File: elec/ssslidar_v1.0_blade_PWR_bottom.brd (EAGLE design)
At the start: 12 x 7 mm, 25 parts, among them P10 PIN_SMD_1X1_RECT, P11 PIN_SMD_1X2, P12 PIN_SMD_1X1_RECT, P13 PIN_SMD_1X1_RECT, P15 PIN_SMD_0.8X1_RECT, P16 PIN_SMD_1X1_RECT, P17 PIN_SMD_1X2, P18 PIN_SMD_0.8X1_RECT, P19 PIN_SMD_0.8X1_RECT, P2 PIN_SMD_1X1_RECT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

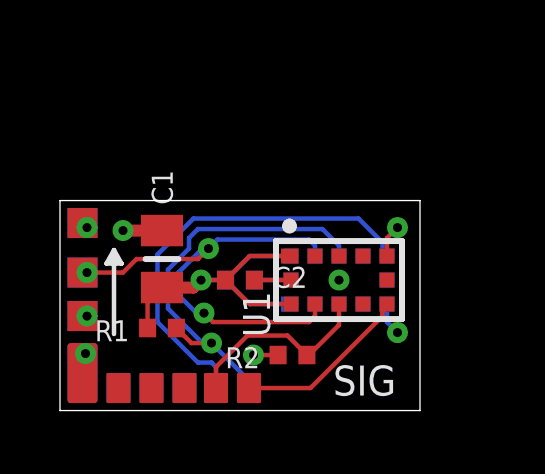
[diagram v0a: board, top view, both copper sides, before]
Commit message: Separated blades into bottom and top, since the bottom ones need to be taller to avoid seeing the Main PCB, or the screws...
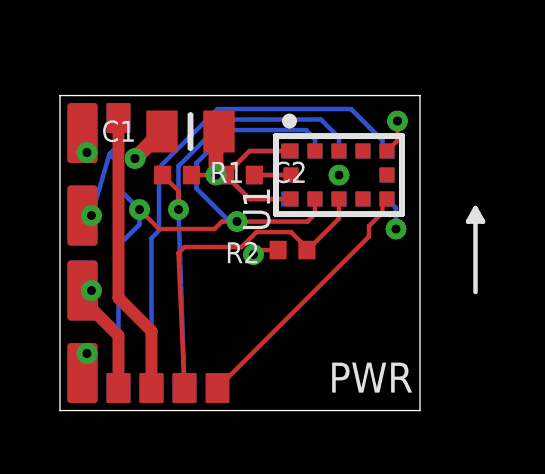
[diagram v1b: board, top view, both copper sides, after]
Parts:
- removed P19, P20, P23: PIN_SMD_0.8X1_RECT, Xevelabs:PIN_SMD_0.8X1_RECT
- added P1, P3: PIN_SMD_0.8X1_RECT, Xevelabs:PIN_SMD_0.8X1_RECT
- P10, P12, P13, P16, P2, P9: value PIN_SMD_1X1_RECT -> PIN_SMD_1X2; device Xevelabs:PIN_SMD_1X1_RECT -> Xevelabs:PIN_SMD_1X2
- moved P18 9.26 mm to (1.95, 9.75), turned to 90 degrees
- moved R1 5.12 mm to (3.90, 7.85), turned to 0 degrees
- moved C1 4.35 mm to (4.35, 9.30), turned to 180 degrees
- moved C2 3.50 mm to (6.00, 7.85)
- moved C3 3.50 mm to (6.00, 7.85)
- moved U1 3.50 mm to (9.30, 7.85)
- moved U2 3.50 mm to (9.30, 7.85)
- moved R2 3.50 mm to (7.75, 5.35)
- moved P2 3.00 mm to (0.75, 9.25), turned to 0 degrees
- moved P9 3.00 mm to (0.75, 9.25)
- moved P7 2.15 mm to (3.05, 0.75)
- moved P5 2.15 mm to (4.15, 0.75)
- moved P10 1.90 mm to (0.75, 6.50)
- moved P12 1.90 mm to (0.75, 6.50)
- moved P8 1.10 mm to (1.95, 0.75), flipped to the top, turned to 90 degrees
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- renumbered P15 to P14
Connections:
- new net VDD_PASS: P1.PIN, P14.PIN
- net GND: now also P2.P$1, P9.P$1; no longer P2.PIN, P9.PIN
- net SCL: now also P10.P$1, P12.P$1, P18.PIN, P3.PIN; no longer P10.PIN, P12.PIN
- net VDD: now also P13.P$1, P16.P$1, P8.PIN; no longer P13.PIN, P16.PIN
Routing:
- net SCL: track 16.3 -> 27.0 mm
- net VDD_PASS: track 0.00 -> 9.46 mm
- net SDA1: track 6.62 -> 11.5 mm
- net INT1: track 5.91 -> 8.64 mm
- net VDD: track 17.9 -> 20.6 mm
- net INT2: track 14.4 -> 16.6 mm
- net SDA2: track 13.7 -> 15.5 mm
- net GND: track 5.66 -> 7.16 mm
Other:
- board size 12 x 7 mm -> 12 x 10.5 mm
- board text added: "PWR"
- board text removed: "SIG"

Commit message: Blades redesign done.
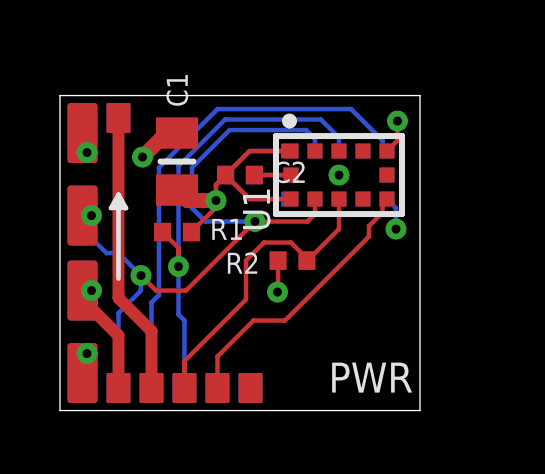
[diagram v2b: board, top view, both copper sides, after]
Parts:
- added P15, P19, P20: PIN_SMD_0.8X1_RECT, Xevelabs:PIN_SMD_0.8X1_RECT
- moved R1 1.90 mm to (3.90, 5.95)
- moved C1 1.10 mm to (3.90, 8.30), turned to 90 degrees
- moved R2 0.35 mm to (7.75, 5.00)
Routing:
- net VDD: track 20.6 -> 22.3 mm
- net SCL: track 27.0 -> 28.4 mm
- net SDA1: track 11.5 -> 10.2 mm
- net INT1: track 8.64 -> 9.26 mm

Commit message: Updated all libs.
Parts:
- turned P10 to 90 degrees
- turned P11 to 270 degrees
- turned P12 to 90 degrees
- turned P13 to 270 degrees
- turned P16 to 270 degrees
- turned P17 to 270 degrees
- turned P2 to 270 degrees
- turned P9 to 90 degrees
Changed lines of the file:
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@@
 <element name="U2" library="VL53L0X" package="VL53L0X" value="VL53L0X" x="9.3" y="7.85" rot="MR270"/>
 <element name="P1" library="Xevelabs" package="PIN_SMD_0.8X1_RECT" value="PIN_SMD_0.8X1_RECT" x="1.95" y="9.75" rot="R90"/>
-<element name="P2" library="Xevelabs" package="PIN_SMD_1X2" value="PIN_SMD_1X2" x="0.75" y="9.25" rot="MR0"/>
+<element name="P2" library="Xevelabs" package="PIN_SMD_1X2" value="PIN_SMD_1X2" x="0.75" y="9.25" rot="MR270"/>
 <element name="P3" library="Xevelabs" package="PIN_SMD_0.8X1_RECT" value="PIN_SMD_0.8X1_RECT" x="1.95" y="0.75" rot="MR90"/>
 <element name="P4" library="Xevelabs" package="PIN_SMD_0.8X1_RECT" value="PIN_SMD_0.8X1_RECT" x="4.15" y="0.75" rot="R90"/>
@@
 <element name="P6" library="Xevelabs" package="PIN_SMD_0.8X1_RECT" value="PIN_SMD_0.8X1_RECT" x="5.25" y="0.75" rot="R90"/>
 <element name="P7" library="Xevelabs" package="PIN_SMD_0.8X1_RECT" value="PIN_SMD_0.8X1_RECT" x="3.05" y="0.75" rot="MR90"/>
-<element name="P16" library="Xevelabs" package="PIN_SMD_1X2" value="PIN_SMD_1X2" x="0.75" y="4" rot="R180"/>
-<element name="P17" library="Xevelabs" package="PIN_SMD_1X2" value="PIN_SMD_1X2" x="0.75" y="1.25" rot="MR0"/>
+<element name="P16" library="Xevelabs" package="PIN_SMD_1X2" value="PIN_SMD_1X2" x="0.75" y="4" rot="R270"/>
+<element name="P17" library="Xevelabs" package="PIN_SMD_1X2" value="PIN_SMD_1X2" x="0.75" y="1.25" rot="MR270"/>
 <element name="P18" library="Xevelabs" package="PIN_SMD_0.8X1_RECT" value="PIN_SMD_0.8X1_RECT" x="1.95" y="9.75" rot="MR90"/>
 <element name="P8" library="Xevelabs" package="PIN_SMD_0.8X1_RECT" value="PIN_SMD_0.8X1_RECT" x="1.95" y="0.75" rot="R90"/>
-<element name="P9" library="Xevelabs" package="PIN_SMD_1X2" value="PIN_SMD_1X2" x="0.75" y="9.25"/>
-<element name="P10" library="Xevelabs" package="PIN_SMD_1X2" value="PIN_SMD_1X2" x="0.75" y="6.5" rot="MR180"/>
-<element name="P11" library="Xevelabs" package="PIN_SMD_1X2" value="PIN_SMD_1X2" x="0.75" y="1.25" rot="R180"/>
-<element name="P12" library="Xevelabs" package="PIN_SMD_1X2" value="PIN_SMD_1X2" x="0.75" y="6.5"/>
-<element name="P13" library="Xevelabs" package="PIN_SMD_1X2" value="PIN_SMD_1X2" x="0.75" y="4" rot="MR0"/>
+<element name="P9" library="Xevelabs" package="PIN_SMD_1X2" value="PIN_SMD_1X2" x="0.75" y="9.25" rot="R90"/>
+<element name="P10" library="Xevelabs" package="PIN_SMD_1X2" value="PIN_SMD_1X2" x="0.75" y="6.5" rot="MR90"/>
+<element name="P11" library="Xevelabs" package="PIN_SMD_1X2" value="PIN_SMD_1X2" x="0.75" y="1.25" rot="R270"/>
+<element name="P12" library="Xevelabs" package="PIN_SMD_1X2" value="PIN_SMD_1X2" x="0.75" y="6.5" rot="R90"/>
+<element name="P13" library="Xevelabs" package="PIN_SMD_1X2" value="PIN_SMD_1X2" x="0.75" y="4" rot="MR270"/>
 <element name="R1" library="Xevelabs" package="0402_N" value="2k" x="3.9" y="5.95"/>
 <element name="R2" library="Xevelabs" package="0402_N" value="2k" x="7.75" y="5" rot="R180"/>
